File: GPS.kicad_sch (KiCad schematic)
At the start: 17 parts

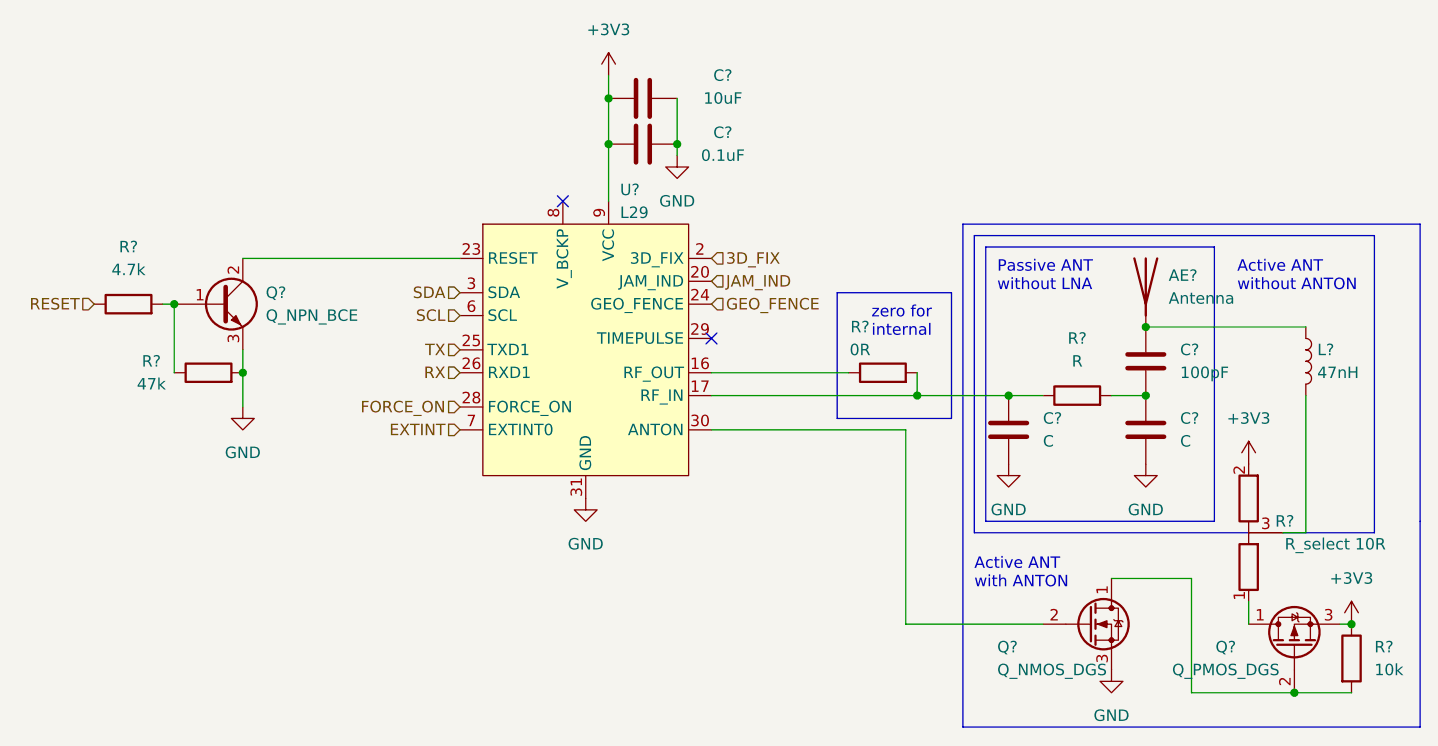
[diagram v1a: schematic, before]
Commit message: added audio ref schematic, added bat to 5V, added shift register, connected devices with other periferals
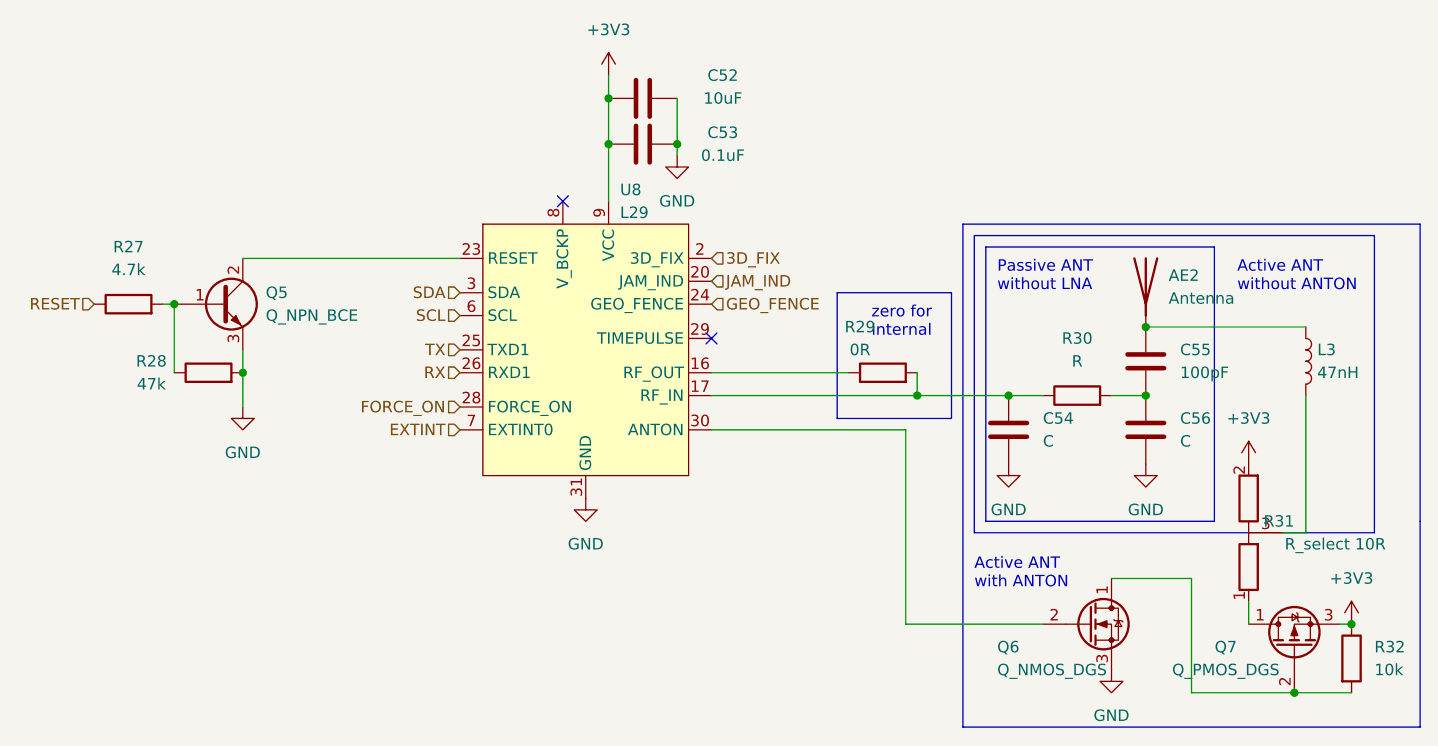
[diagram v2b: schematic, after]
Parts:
- gave numbers to parts that had none: 17
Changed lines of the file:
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@@
   (symbol (lib_id "Device:R") (at 172.72 90.17 90) (unit 1)
     (in_bom yes) (on_board yes)
-    (property "Reference" "R?" (id 0) (at 170.18 85.09 90))
+    (property "Reference" "R29" (id 0) (at 170.18 85.09 90))
     (property "Value" "0R" (id 1) (at 170.18 87.63 90))
     (property "Footprint" "" (id 2) (at 172.72 91.948 90)
@@
   (symbol (lib_id "airsoft_controller:L29") (at 139.7 87.63 0) (unit 1)
     (in_bom yes) (on_board yes)
-    (property "Reference" "U?" (id 0) (at 143.51 69.85 0)
+    (property "Reference" "U8" (id 0) (at 143.51 69.85 0)
       (effects (font (size 1.27 1.27)) (justify left))
     )
@@
   (symbol (lib_id "Device:C") (at 201.93 88.9 180) (unit 1)
     (in_bom yes) (on_board yes)
-    (property "Reference" "C?" (id 0) (at 205.74 87.6299 0)
+    (property "Reference" "C55" (id 0) (at 205.74 87.6299 0)
       (effects (font (size 1.27 1.27)) (justify right))
     )
@@
   (symbol (lib_id "Device:C") (at 146.05 64.77 270) (mirror x) (unit 1)
     (in_bom yes) (on_board yes)
-    (property "Reference" "C?" (id 0) (at 154.94 63.5 90))
+    (property "Reference" "C53" (id 0) (at 154.94 63.5 90))
     (property "Value" "0.1uF" (id 1) (at 154.94 66.04 90))
     (property "Footprint" "" (id 2) (at 142.24 63.8048 0)
@@
   (symbol (lib_id "Device:Antenna") (at 201.93 80.01 0) (unit 1)
     (in_bom yes) (on_board yes) (fields_autoplaced)
-    (property "Reference" "AE?" (id 0) (at 204.47 79.3749 0)
+    (property "Reference" "AE2" (id 0) (at 204.47 79.3749 0)
       (effects (font (size 1.27 1.27)) (justify left))
     )
@@
   (symbol (lib_id "Device:C") (at 201.93 96.52 0) (unit 1)
     (in_bom yes) (on_board yes) (fields_autoplaced)
-    (property "Reference" "C?" (id 0) (at 205.74 95.2499 0)
+    (property "Reference" "C56" (id 0) (at 205.74 95.2499 0)
       (effects (font (size 1.27 1.27)) (justify left))
     )
@@
   (symbol (lib_id "Device:Q_NMOS_DGS") (at 195.58 118.11 0) (unit 1)
     (in_bom yes) (on_board yes)
-    (property "Reference" "Q?" (id 0) (at 185.42 120.65 0)
+    (property "Reference" "Q6" (id 0) (at 185.42 120.65 0)
       (effects (font (size 1.27 1.27)) (justify left))
     )
@@
   (symbol (lib_id "airsoft_controller:R_select") (at 213.36 107.95 180) (unit 1)
     (in_bom yes) (on_board yes)
-    (property "Reference" "R?" (id 0) (at 218.44 106.68 0)
+    (property "Reference" "R31" (id 0) (at 218.44 106.68 0)
       (effects (font (size 1.27 1.27)) (justify left))
     )
@@
   (symbol (lib_id "Device:C") (at 186.69 96.52 0) (unit 1)
     (in_bom yes) (on_board yes) (fields_autoplaced)
-    (property "Reference" "C?" (id 0) (at 190.5 95.2499 0)
+    (property "Reference" "C54" (id 0) (at 190.5 95.2499 0)
       (effects (font (size 1.27 1.27)) (justify left))
     )
@@
   (symbol (lib_id "Device:Q_NPN_BCE") (at 99.06 82.55 0) (unit 1)
     (in_bom yes) (on_board yes) (fields_autoplaced)
-    (property "Reference" "Q?" (id 0) (at 104.14 81.2799 0)
+    (property "Reference" "Q5" (id 0) (at 104.14 81.2799 0)
       (effects (font (size 1.27 1.27)) (justify left))
     )
@@
   (symbol (lib_id "Device:Q_PMOS_DGS") (at 218.44 120.65 90) (unit 1)
     (in_bom yes) (on_board yes)
-    (property "Reference" "Q?" (id 0) (at 210.82 120.65 90))
+    (property "Reference" "Q7" (id 0) (at 210.82 120.65 90))
     (property "Value" "Q_PMOS_DGS" (id 1) (at 210.82 123.19 90))
     (property "Footprint" "" (id 2) (at 215.9 115.57 0)
@@
   (symbol (lib_id "Device:R") (at 97.79 90.17 90) (unit 1)
     (in_bom yes) (on_board yes)
-    (property "Reference" "R?" (id 0) (at 91.44 88.9 90))
+    (property "Reference" "R28" (id 0) (at 91.44 88.9 90))
     (property "Value" "47k" (id 1) (at 91.44 91.44 90))
     (property "Footprint" "" (id 2) (at 97.79 91.948 90)
@@
   (symbol (lib_id "Device:C") (at 146.05 59.69 270) (mirror x) (unit 1)
     (in_bom yes) (on_board yes)
-    (property "Reference" "C?" (id 0) (at 154.94 57.15 90))
+    (property "Reference" "C52" (id 0) (at 154.94 57.15 90))
     (property "Value" "10uF" (id 1) (at 154.94 59.69 90))
     (property "Footprint" "" (id 2) (at 142.24 58.7248 0)
@@
   (symbol (lib_id "Device:L") (at 219.71 88.9 0) (unit 1)
     (in_bom yes) (on_board yes) (fields_autoplaced)
-    (property "Reference" "L?" (id 0) (at 220.98 87.6299 0)
+    (property "Reference" "L3" (id 0) (at 220.98 87.6299 0)
       (effects (font (size 1.27 1.27)) (justify left))
     )
@@
   (symbol (lib_id "Device:R") (at 224.79 121.92 0) (unit 1)
     (in_bom yes) (on_board yes) (fields_autoplaced)
-    (property "Reference" "R?" (id 0) (at 227.33 120.6499 0)
+    (property "Reference" "R32" (id 0) (at 227.33 120.6499 0)
       (effects (font (size 1.27 1.27)) (justify left))
     )
@@
   (symbol (lib_id "Device:R") (at 88.9 82.55 90) (unit 1)
     (in_bom yes) (on_board yes) (fields_autoplaced)
-    (property "Reference" "R?" (id 0) (at 88.9 76.2 90))
+    (property "Reference" "R27" (id 0) (at 88.9 76.2 90))
     (property "Value" "4.7k" (id 1) (at 88.9 78.74 90))
     (property "Footprint" "" (id 2) (at 88.9 84.328 90)
@@
   (symbol (lib_id "Device:R") (at 194.31 92.71 90) (unit 1)
     (in_bom yes) (on_board yes) (fields_autoplaced)
-    (property "Reference" "R?" (id 0) (at 194.31 86.36 90))
+    (property "Reference" "R30" (id 0) (at 194.31 86.36 90))
     (property "Value" "R" (id 1) (at 194.31 88.9 90))
     (property "Footprint" "" (id 2) (at 194.31 94.488 90)

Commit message: added adcin2 config description, fixed some rule check errors
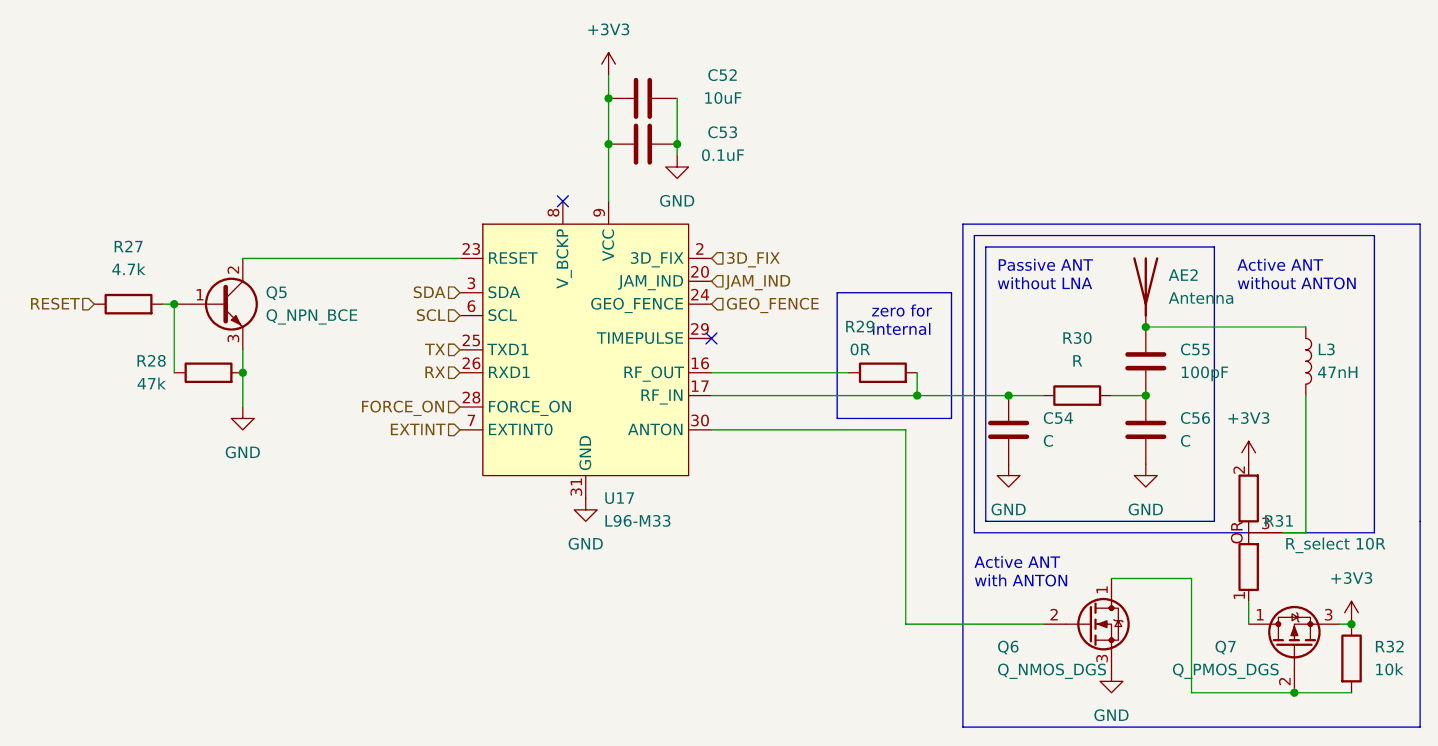
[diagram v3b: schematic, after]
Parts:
- removed U8: L29, airsoft_controller:L29, symbol airsoft_controller:L29
- added U17: L96-M33, airsoft_controller:L29, symbol airsoft_controller:L96-M33
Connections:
- net +3V3: now also U17.9 (VCC)
- net 3D_FIX: now also U17.2 (3D_FIX)
- net EXTINT: now also U17.7 (EXTINT0)
- net FORCE_ON: now also U17.28 (FORCE_ON)
- net GEO_FENCE: now also U17.24 (GEO_FENCE)
- net GND: now also U17.10 (GND), U17.11 (GND), U17.12 (GND), U17.13 (GND), U17.14 (GND), U17.15 (GND), U17.18 (GND), U17.19 (GND), U17.21 (GND), U17.22 (GND), U17.27 (GND), U17.31 (GND), U17.4 (GND), U17.5 (GND)
- net JAM_IND: now also U17.20 (JAM_IND)
- net RX: now also U17.26 (RXD1)
- net SCL: now also U17.6 (SCL)
- net SDA: now also U17.3 (SDA)
- net TX: now also U17.25 (TXD1)
- net at R29.1: now also U17.16 (RF_OUT)
- net at C54.1, R29.2, R30.1: now also U17.17 (RF_IN)
- net at Q5.2 (C): now also U17.23 (RESET)
- net at Q6.2 (G): now also U17.30 (ANTON)
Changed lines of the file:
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@@
     (pin "2")
-  )
-  (symbol (lib_id "airsoft_controller:L29") (at 139.7 87.63 0) (unit 1)
-    (in_bom yes) (on_board yes)
-    (property "Reference" "U8" (id 0) (at 143.51 69.85 0)
-      (effects (font (size 1.27 1.27)) (justify left))
-    )
-    (property "Value" "L29" (id 1) (at 143.51 72.39 0)
-      (effects (font (size 1.27 1.27)) (justify left))
-    )
-    (property "Footprint" "airsoft_controller:L29" (id 2) (at 140.97 106.68 0)
-      (effects (font (size 1.27 1.27)) hide)
-    )
-    (property "Datasheet" "" (id 3) (at 139.7 87.63 0)
-      (effects (font (size 1.27 1.27)) hide)
-    )
-    (pin "1")
-    (pin "10")
-    (pin "11")
-    (pin "12")
-    (pin "13")
-    (pin "14")
-    (pin "15")
-    (pin "16")
-    (pin "17")
-    (pin "18")
-    (pin "19")
-    (pin "2")
-    (pin "20")
-    (pin "21")
-    (pin "22")
-    (pin "23")
-    (pin "24")
-    (pin "25")
-    (pin "26")
-    (pin "27")
-    (pin "28")
-    (pin "29")
-    (pin "3")
-    (pin "30")
-    (pin "31")
-    (pin "4")
-    (pin "5")
-    (pin "6")
-    (pin "7")
-    (pin "8")
-    (pin "9")
   )
   (symbol (lib_id "power:GND") (at 201.93 100.33 0) (unit 1)
@@
     (pin "3")
   )
+  (symbol (lib_id "airsoft_controller:L96-M33") (at 139.7 87.63 0) (unit 1)
+    (in_bom yes) (on_board yes) (fields_autoplaced)
+    (property "Reference" "U17" (id 0) (at 141.7194 104.14 0)
+      (effects (font (size 1.27 1.27)) (justify left))
+    )
+    (property "Value" "L96-M33" (id 1) (at 141.7194 106.68 0)
+      (effects (font (size 1.27 1.27)) (justify left))
+    )
+    (property "Footprint" "airsoft_controller:L29" (id 2) (at 140.97 106.68 0)
+      (effects (font (size 1.27 1.27)) hide)
+    )
+    (property "Datasheet" "" (id 3) (at 139.7 87.63 0)
+      (effects (font (size 1.27 1.27)) hide)
+    )
+    (pin "1")
+    (pin "10")
+    (pin "11")
+    (pin "12")
+    (pin "13")
+    (pin "14")
+    (pin "15")
+    (pin "16")
+    (pin "17")
+    (pin "18")
+    (pin "19")
+    (pin "2")
+    (pin "20")
+    (pin "21")
+    (pin "22")
+    (pin "23")
+    (pin "24")
+    (pin "25")
+    (pin "26")
+    (pin "27")
+    (pin "28")
+    (pin "29")
+    (pin "3")
+    (pin "30")
+    (pin "31")
+    (pin "4")
+    (pin "5")
+    (pin "6")
+    (pin "7")
+    (pin "8")
+    (pin "9")
+  )
   (symbol (lib_id "power:GND") (at 186.69 100.33 0) (unit 1)

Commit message: minor optimized pinassignement, added capacitors, added connectors
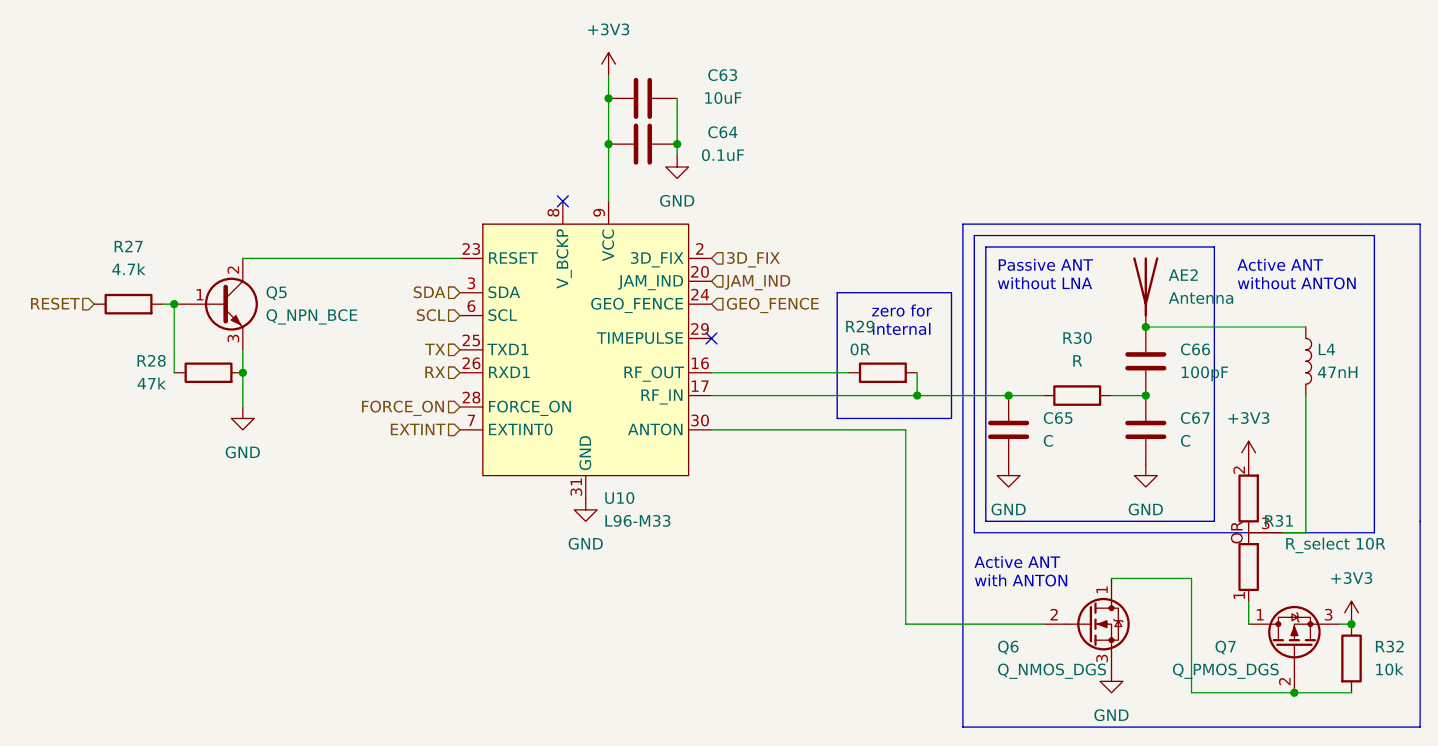
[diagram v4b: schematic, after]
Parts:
- renumbered C52 to C63, C53 to C64, C54 to C65, C55 to C66, C56 to C67, L3 to L4, U17 to U10
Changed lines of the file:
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@@
   (symbol (lib_id "power:GND") (at 201.93 100.33 0) (unit 1)
     (in_bom yes) (on_board yes) (fields_autoplaced)
-    (property "Reference" "#PWR0168" (id 0) (at 201.93 106.68 0)
+    (property "Reference" "#PWR083" (id 0) (at 201.93 106.68 0)
       (effects (font (size 1.27 1.27)) hide)
     )
@@
   (symbol (lib_id "Device:C") (at 201.93 88.9 180) (unit 1)
     (in_bom yes) (on_board yes)
-    (property "Reference" "C55" (id 0) (at 205.74 87.6299 0)
+    (property "Reference" "C66" (id 0) (at 205.74 87.6299 0)
       (effects (font (size 1.27 1.27)) (justify right))
     )
@@
   (symbol (lib_id "power:+3V3") (at 213.36 100.33 0) (unit 1)
     (in_bom yes) (on_board yes) (fields_autoplaced)
-    (property "Reference" "#PWR0165" (id 0) (at 213.36 104.14 0)
+    (property "Reference" "#PWR084" (id 0) (at 213.36 104.14 0)
       (effects (font (size 1.27 1.27)) hide)
     )
@@
   (symbol (lib_id "Device:C") (at 146.05 64.77 270) (mirror x) (unit 1)
     (in_bom yes) (on_board yes)
-    (property "Reference" "C53" (id 0) (at 154.94 63.5 90))
+    (property "Reference" "C64" (id 0) (at 154.94 63.5 90))
     (property "Value" "0.1uF" (id 1) (at 154.94 66.04 90))
     (property "Footprint" "" (id 2) (at 142.24 63.8048 0)
@@
   (symbol (lib_id "Device:C") (at 201.93 96.52 0) (unit 1)
     (in_bom yes) (on_board yes) (fields_autoplaced)
-    (property "Reference" "C56" (id 0) (at 205.74 95.2499 0)
+    (property "Reference" "C67" (id 0) (at 205.74 95.2499 0)
       (effects (font (size 1.27 1.27)) (justify left))
     )
@@
   (symbol (lib_id "airsoft_controller:L96-M33") (at 139.7 87.63 0) (unit 1)
     (in_bom yes) (on_board yes) (fields_autoplaced)
-    (property "Reference" "U17" (id 0) (at 141.7194 104.14 0)
+    (property "Reference" "U10" (id 0) (at 141.7194 104.14 0)
       (effects (font (size 1.27 1.27)) (justify left))
     )
@@
   (symbol (lib_id "power:GND") (at 186.69 100.33 0) (unit 1)
     (in_bom yes) (on_board yes) (fields_autoplaced)
-    (property "Reference" "#PWR0167" (id 0) (at 186.69 106.68 0)
+    (property "Reference" "#PWR081" (id 0) (at 186.69 106.68 0)
       (effects (font (size 1.27 1.27)) hide)
     )
@@
   (symbol (lib_id "Device:C") (at 186.69 96.52 0) (unit 1)
     (in_bom yes) (on_board yes) (fields_autoplaced)
-    (property "Reference" "C54" (id 0) (at 190.5 95.2499 0)
+    (property "Reference" "C65" (id 0) (at 190.5 95.2499 0)
       (effects (font (size 1.27 1.27)) (justify left))
     )
@@
   (symbol (lib_id "power:GND") (at 139.7 104.14 0) (unit 1)
     (in_bom yes) (on_board yes) (fields_autoplaced)
-    (property "Reference" "#PWR0160" (id 0) (at 139.7 110.49 0)
+    (property "Reference" "#PWR078" (id 0) (at 139.7 110.49 0)
       (effects (font (size 1.27 1.27)) hide)
     )
@@
   (symbol (lib_id "power:+3V3") (at 142.24 57.15 0) (mirror y) (unit 1)
     (in_bom yes) (on_board yes) (fields_autoplaced)
-    (property "Reference" "#PWR0162" (id 0) (at 142.24 60.96 0)
+    (property "Reference" "#PWR079" (id 0) (at 142.24 60.96 0)
       (effects (font (size 1.27 1.27)) hide)
     )
@@
   (symbol (lib_id "power:GND") (at 101.6 93.98 0) (unit 1)
     (in_bom yes) (on_board yes) (fields_autoplaced)
-    (property "Reference" "#PWR0163" (id 0) (at 101.6 100.33 0)
+    (property "Reference" "#PWR077" (id 0) (at 101.6 100.33 0)
       (effects (font (size 1.27 1.27)) hide)
     )
@@
   (symbol (lib_id "Device:C") (at 146.05 59.69 270) (mirror x) (unit 1)
     (in_bom yes) (on_board yes)
-    (property "Reference" "C52" (id 0) (at 154.94 57.15 90))
+    (property "Reference" "C63" (id 0) (at 154.94 57.15 90))
     (property "Value" "10uF" (id 1) (at 154.94 59.69 90))
     (property "Footprint" "" (id 2) (at 142.24 58.7248 0)
@@
   (symbol (lib_id "Device:L") (at 219.71 88.9 0) (unit 1)
     (in_bom yes) (on_board yes) (fields_autoplaced)
-    (property "Reference" "L3" (id 0) (at 220.98 87.6299 0)
+    (property "Reference" "L4" (id 0) (at 220.98 87.6299 0)
       (effects (font (size 1.27 1.27)) (justify left))
     )
@@
   (symbol (lib_id "power:GND") (at 149.86 66.04 0) (mirror y) (unit 1)
     (in_bom yes) (on_board yes) (fields_autoplaced)
-    (property "Reference" "#PWR0161" (id 0) (at 149.86 72.39 0)
+    (property "Reference" "#PWR080" (id 0) (at 149.86 72.39 0)
       (effects (font (size 1.27 1.27)) hide)
     )
@@
   (symbol (lib_id "power:+3V3") (at 224.79 118.11 0) (unit 1)
     (in_bom yes) (on_board yes) (fields_autoplaced)
-    (property "Reference" "#PWR0164" (id 0) (at 224.79 121.92 0)
+    (property "Reference" "#PWR085" (id 0) (at 224.79 121.92 0)
       (effects (font (size 1.27 1.27)) hide)
     )
@@
   (symbol (lib_id "power:GND") (at 198.12 123.19 0) (unit 1)
     (in_bom yes) (on_board yes) (fields_autoplaced)
-    (property "Reference" "#PWR0166" (id 0) (at 198.12 129.54 0)
-      (effects (font (size 1.27 1.27)) hide)
-    )
+    (property "Reference" "#PWR082" (id 0) (at 198.12 129.54 0)
+      (effects (font (size 1.27 1.27)) hide)
+    )
